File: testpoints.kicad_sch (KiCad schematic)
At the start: 41 parts

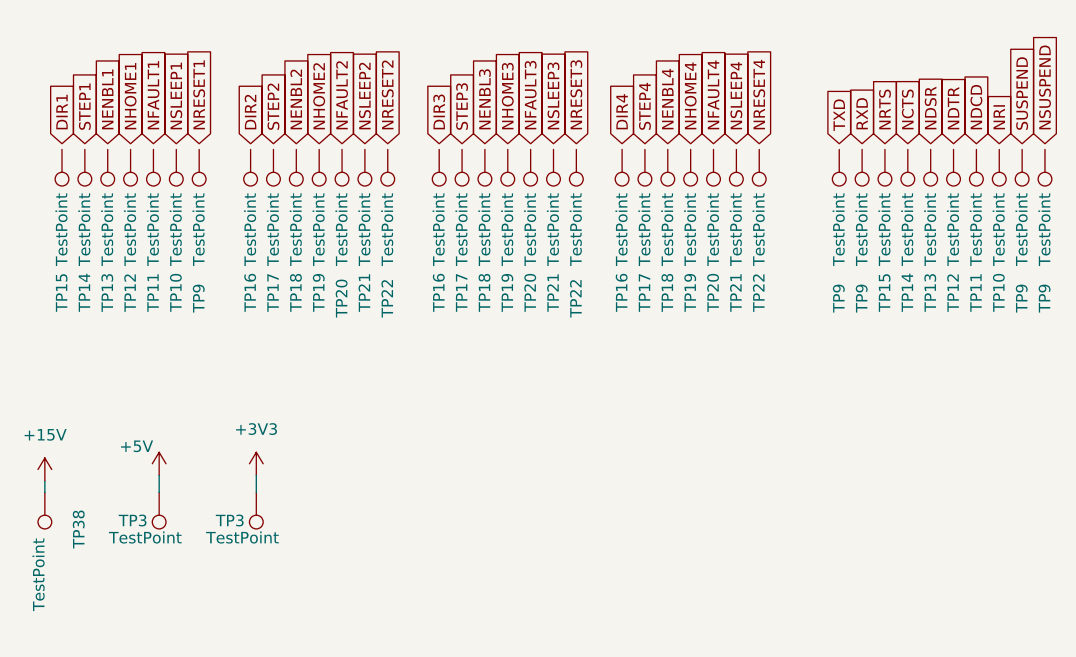
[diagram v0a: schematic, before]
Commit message: routet Motor Driver modules, reattached and placed testpoints
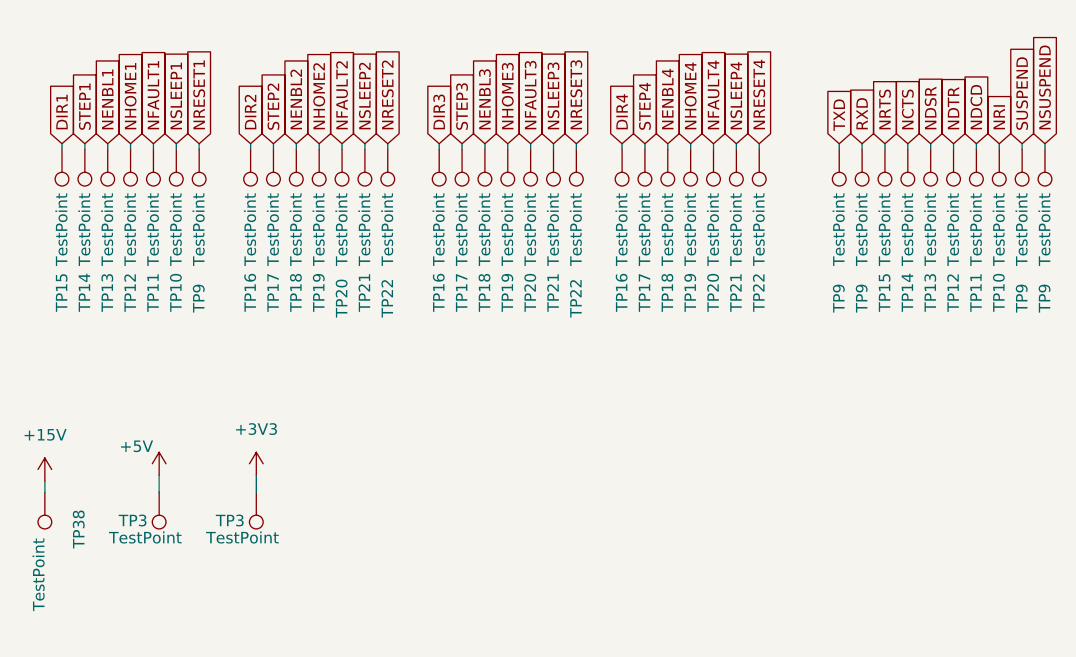
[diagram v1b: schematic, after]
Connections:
- net DIR1: now also TP15.1
- net DIR2: now also TP16.1
- net DIR3: now also TP16.1
- net DIR4: now also TP16.1
- net NCTS: now also TP14.1
- net NDCD: now also TP11.1
- net NDSR: now also TP13.1
- net NDTR: now also TP12.1
- net NENBL1: now also TP13.1
- net NENBL2: now also TP18.1
- net NENBL3: now also TP18.1
- net NENBL4: now also TP18.1
- net NFAULT1: now also TP11.1
- net NFAULT2: now also TP20.1
- net NFAULT3: now also TP20.1
- net NFAULT4: now also TP20.1
- net NHOME1: now also TP12.1
- net NHOME2: now also TP19.1
- net NHOME3: now also TP19.1
- net NHOME4: now also TP19.1
- net NRESET1: now also TP9.1
- net NRESET2: now also TP22.1
- net NRESET3: now also TP22.1
- net NRESET4: now also TP22.1
- net NRI: now also TP10.1
- net NRTS: now also TP15.1
- net NSLEEP1: now also TP10.1
- net NSLEEP2: now also TP21.1
- net NSLEEP3: now also TP21.1
- net NSLEEP4: now also TP21.1
- net NSUSPEND: now also TP9.1
- net RXD: now also TP9.1
- net STEP1: now also TP14.1
- net STEP2: now also TP17.1
- net STEP3: now also TP17.1
- net STEP4: now also TP17.1
- net SUSPEND: now also TP9.1
- net TXD: now also TP9.1
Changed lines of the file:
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@@
 (kicad_sch (version 20230121) (generator eeschema)
   (paper "A4")
+  (wire (pts (xy 53.34 92.71) (xy 53.34 93.345))
+    (stroke (width 0) (type default))
+  )
+  (wire (pts (xy 85.09 92.71) (xy 85.09 93.345))
+    (stroke (width 0) (type default))
+  )
+  (wire (pts (xy 142.24 92.71) (xy 142.24 93.345))
+    (stroke (width 0) (type default))
+  )
+  (wire (pts (xy 64.135 92.71) (xy 64.135 93.345))
+    (stroke (width 0) (type default))
+  )
+  (wire (pts (xy 71.755 92.71) (xy 71.755 93.345))
+    (stroke (width 0) (type default))
+  )
+  (wire (pts (xy 152.4 92.71) (xy 152.4 93.345))
+    (stroke (width 0) (type default))
+  )
+  (wire (pts (xy 55.88 92.71) (xy 55.88 93.345))
+    (stroke (width 0) (type default))
+  )
+  (wire (pts (xy 76.835 92.71) (xy 76.835 93.345))
+    (stroke (width 0) (type default))
+  )
+  (wire (pts (xy 107.95 92.71) (xy 107.95 93.345))
+    (stroke (width 0) (type default))
+  )
+  (wire (pts (xy 50.8 92.71) (xy 50.8 93.345))
+    (stroke (width 0) (type default))
+  )
+  (wire (pts (xy 134.62 92.71) (xy 134.62 93.345))
+    (stroke (width 0) (type default))
+  )
   (wire (pts (xy 53.975 131.445) (xy 53.975 129.54))
+    (stroke (width 0) (type default))
+  )
+  (wire (pts (xy 95.25 92.71) (xy 95.25 93.345))
+    (stroke (width 0) (type default))
+  )
+  (wire (pts (xy 97.79 92.71) (xy 97.79 93.345))
+    (stroke (width 0) (type default))
+  )
+  (wire (pts (xy 100.33 92.71) (xy 100.33 93.345))
+    (stroke (width 0) (type default))
+  )
+  (wire (pts (xy 79.375 92.71) (xy 79.375 93.345))
     (stroke (width 0) (type default))
   )
@@
     (stroke (width 0) (type default))
   )
+  (wire (pts (xy 129.54 92.71) (xy 129.54 93.345))
+    (stroke (width 0) (type default))
+  )
+  (wire (pts (xy 74.295 92.71) (xy 74.295 93.345))
+    (stroke (width 0) (type default))
+  )
+  (wire (pts (xy 147.32 92.71) (xy 147.32 93.345))
+    (stroke (width 0) (type default))
+  )
+  (wire (pts (xy 43.18 92.71) (xy 43.18 93.345))
+    (stroke (width 0) (type default))
+  )
+  (wire (pts (xy 69.215 92.71) (xy 69.215 93.345))
+    (stroke (width 0) (type default))
+  )
+  (wire (pts (xy 45.72 92.71) (xy 45.72 93.345))
+    (stroke (width 0) (type default))
+  )
+  (wire (pts (xy 118.11 92.71) (xy 118.11 93.345))
+    (stroke (width 0) (type default))
+  )
+  (wire (pts (xy 105.41 92.71) (xy 105.41 93.345))
+    (stroke (width 0) (type default))
+  )
+  (wire (pts (xy 113.03 92.71) (xy 113.03 93.345))
+    (stroke (width 0) (type default))
+  )
+  (wire (pts (xy 110.49 92.71) (xy 110.49 93.345))
+    (stroke (width 0) (type default))
+  )
+  (wire (pts (xy 137.16 92.71) (xy 137.16 93.345))
+    (stroke (width 0) (type default))
+  )
+  (wire (pts (xy 66.675 92.71) (xy 66.675 93.345))
+    (stroke (width 0) (type default))
+  )
+  (wire (pts (xy 58.42 92.71) (xy 58.42 93.345))
+    (stroke (width 0) (type default))
+  )
   (wire (pts (xy 64.77 131.445) (xy 64.77 129.54))
     (stroke (width 0) (type default))
   )
+  (wire (pts (xy 120.65 92.71) (xy 120.65 93.345))
+    (stroke (width 0) (type default))
+  )
+  (wire (pts (xy 115.57 92.71) (xy 115.57 93.345))
+    (stroke (width 0) (type default))
+  )
+  (wire (pts (xy 48.26 92.71) (xy 48.26 93.345))
+    (stroke (width 0) (type default))
+  )
+  (wire (pts (xy 149.86 92.71) (xy 149.86 93.345))
+    (stroke (width 0) (type default))
+  )
+  (wire (pts (xy 139.7 92.71) (xy 139.7 93.345))
+    (stroke (width 0) (type default))
+  )
+  (wire (pts (xy 132.08 92.71) (xy 132.08 93.345))
+    (stroke (width 0) (type default))
+  )
+  (wire (pts (xy 92.71 92.71) (xy 92.71 93.345))
+    (stroke (width 0) (type default))
+  )
+  (wire (pts (xy 87.63 92.71) (xy 87.63 93.345))
+    (stroke (width 0) (type default))
+  )
+  (wire (pts (xy 144.78 92.71) (xy 144.78 93.345))
+    (stroke (width 0) (type default))
+  )
+  (wire (pts (xy 90.17 92.71) (xy 90.17 93.345))
+    (stroke (width 0) (type default))
+  )

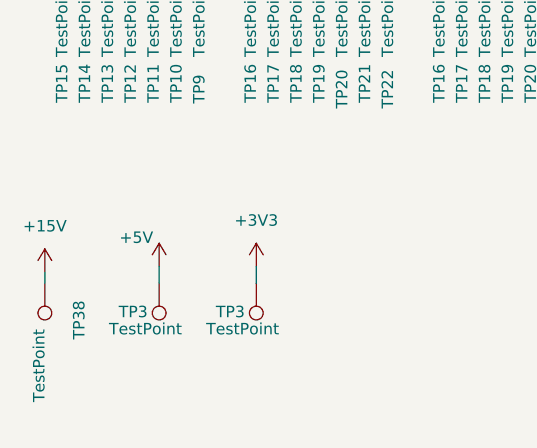
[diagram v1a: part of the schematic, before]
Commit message: finished PCB. DRC 0 errors
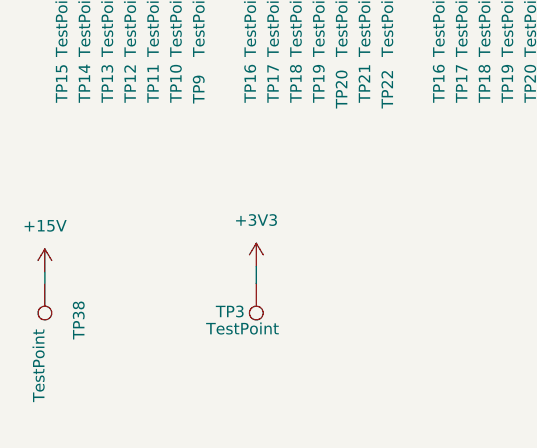
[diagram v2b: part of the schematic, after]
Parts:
- removed TP3: TestPoint, TestPoint:TestPoint_Pad_D2.5mm, symbol Connector:TestPoint
- TP10, TP11, TP12, TP13, TP14, TP15, TP16, TP17, TP18, TP19, TP20, TP21, TP22, TP3, TP38, TP9: footprint TestPoint:TestPoint_Pad_D2.5mm -> TestPoint:TestPoint_Pad_D1.5mm

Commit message: completly reroutet EVERYTHING
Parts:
- removed TP10 (x2), TP11 (x2), TP12 (x2), TP13 (x2), TP14 (x2), TP15 (x2), TP16 (x3), TP17 (x3), TP18 (x3), TP19 (x3), TP20 (x3), TP21 (x3), TP22 (x3), TP3, TP38, TP9 (x5): TestPoint, TestPoint:TestPoint_Pad_D1.5mm, symbol Connector:TestPoint

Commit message: moved every third party content to lib, added 3d models and also just finished rerouting EVERYTHING. also added pcb addon for st-link so i dont accidentally verole anymore
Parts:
- added J4: PINHD_1x4_Male, Connector_PinHeader_2.54mm:PinHeader_1x04_P2.54mm_Vertical, symbol PCM_SL_Pin_Headers:PINHD_1x4_Male
- added J5: USB_A, Connector_USB:USB_A_Stewart_SS-52100-001_Horizontal, symbol Connector:USB_A
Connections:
- new net: J4.1, J5.3 (D+)
- new net: J4.2, J5.4 (GND), J5.5 (Shield)
- new net: J4.3, J5.2 (D-)
- new net: J4.4, J5.1 (VBUS)
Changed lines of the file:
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@@
 (kicad_sch (version 20230121) (generator eeschema)
   (paper "A4")
+  (junction (at 101.6 118.11) (diameter 0) (color 0 0 0 0)
+  )
+  (wire (pts (xy 89.535 111.76) (xy 89.535 101.6))
+    (stroke (width 0) (type default))
+  )
+  (wire (pts (xy 102.87 116.84) (xy 102.87 118.11))
+    (stroke (width 0) (type default))
+  )
+  (wire (pts (xy 101.6 118.11) (xy 100.33 118.11))
+    (stroke (width 0) (type default))
+  )
+  (wire (pts (xy 88.265 104.14) (xy 92.71 104.14))
+    (stroke (width 0) (type default))
+  )
+  (wire (pts (xy 89.535 101.6) (xy 92.71 101.6))
+    (stroke (width 0) (type default))
+  )
+  (wire (pts (xy 88.265 109.22) (xy 92.71 109.22))
+    (stroke (width 0) (type default))
+  )
+  (wire (pts (xy 100.33 118.11) (xy 100.33 116.84))
+    (stroke (width 0) (type default))
+  )
+  (wire (pts (xy 88.265 106.68) (xy 90.805 106.68))
+    (stroke (width 0) (type default))
+  )
+  (wire (pts (xy 92.71 104.14) (xy 92.71 106.68))
+    (stroke (width 0) (type default))
+  )
+  (wire (pts (xy 90.805 106.68) (xy 90.805 120.015))
+    (stroke (width 0) (type default))
+  )
+  (wire (pts (xy 90.805 120.015) (xy 101.6 120.015))
+    (stroke (width 0) (type default))
+  )
+  (wire (pts (xy 101.6 120.015) (xy 101.6 118.11))
+    (stroke (width 0) (type default))
+  )
+  (wire (pts (xy 101.6 118.11) (xy 102.87 118.11))
+    (stroke (width 0) (type default))
+  )
+  (wire (pts (xy 88.265 111.76) (xy 89.535 111.76))
+    (stroke (width 0) (type default))
+  )
+  (symbol (lib_id "PCM_SL_Pin_Headers:PINHD_1x4_Male") (at 84.455 107.95 0) (mirror y) (unit 1)
+    (in_bom yes) (on_board yes) (dnp no) (fields_autoplaced)
+    (property "Reference" "J4" (at 81.915 106.68 0)
+      (effects (font (size 1.27 1.27)) (justify left))
+    )
+    (property "Value" "PINHD_1x4_Male" (at 81.915 109.22 0)
+      (effects (font (size 1.27 1.27)) (justify left))
+    )
+    (property "Footprint" "Connector_PinHeader_2.54mm:PinHeader_1x04_P2.54mm_Vertical" (at 85.725 96.52 0)
+      (effects (font (size 1.27 1.27)) hide)
+    )
+    (property "Datasheet" "" (at 84.455 97.79 0)
+      (effects (font (size 1.27 1.27)) hide)
+    )
+    (pin "3")
+    (pin "4")
+    (pin "2")
+    (pin "1")
+    (instances
+      (project "Doodle Drive"
+        (path "/3ec634aa-8c09-482d-9325-2288a4dbd68b/bef0954e-6024-4756-b9a6-5ea2a0825f13"
+          (reference "J4") (unit 1)
+        )
+      )
+    )
+  )
+  (symbol (lib_id "Connector:USB_A") (at 100.33 106.68 0) (mirror y) (unit 1)
+    (in_bom yes) (on_board yes) (dnp no) (fields_autoplaced)
+    (property "Reference" "J5" (at 100.33 94.615 0)
+      (effects (font (size 1.27 1.27)))
+    )
+    (property "Value" "USB_A" (at 100.33 97.155 0)
+      (effects (font (size 1.27 1.27)))
+    )
+    (property "Footprint" "Connector_USB:USB_A_Stewart_SS-52100-001_Horizontal" (at 96.52 107.95 0)
+      (effects (font (size 1.27 1.27)) hide)
+    )
+    (property "Datasheet" " ~" (at 96.52 107.95 0)
+      (effects (font (size 1.27 1.27)) hide)
+    )
+    (pin "5")
+    (pin "1")
+    (pin "2")
+    (pin "3")
+    (pin "4")
+    (instances
+      (project "Doodle Drive"
+        (path "/3ec634aa-8c09-482d-9325-2288a4dbd68b/bef0954e-6024-4756-b9a6-5ea2a0825f13"
+          (reference "J5") (unit 1)
+        )
+      )
+    )
+  )
 )

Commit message: fixed variuopus stuff, this is probaly the bestellte version
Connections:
- net at J4.1: now also J5.1 (VBUS); no longer J5.3 (D+)
- net at J5.4 (GND), J5.5 (Shield): now also J4.3; no longer J4.2
- net at J5.2 (D-): now also J4.2; no longer J4.3
- net at J4.4: now also J5.3 (D+); no longer J5.1 (VBUS)
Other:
- moved on the sheet: J4
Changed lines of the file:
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@@
     (stroke (width 0) (type default))
   )
-  (wire (pts (xy 88.265 104.14) (xy 92.71 104.14))
+  (wire (pts (xy 88.265 104.14) (xy 92.075 104.14))
     (stroke (width 0) (type default))
   )
@@
     (stroke (width 0) (type default))
   )
-  (wire (pts (xy 92.71 104.14) (xy 92.71 106.68))
+  (wire (pts (xy 92.075 104.14) (xy 92.075 106.68))
     (stroke (width 0) (type default))
   )
@@
     (stroke (width 0) (type default))
   )
+  (wire (pts (xy 92.075 106.68) (xy 92.71 106.68))
+    (stroke (width 0) (type default))
+  )
   (wire (pts (xy 88.265 111.76) (xy 89.535 111.76))
     (stroke (width 0) (type default))
   )
-  (symbol (lib_id "PCM_SL_Pin_Headers:PINHD_1x4_Male") (at 84.455 107.95 0) (mirror y) (unit 1)
-    (in_bom yes) (on_board yes) (dnp no) (fields_autoplaced)
-    (property "Reference" "J4" (at 81.915 106.68 0)
+  (symbol (lib_id "PCM_SL_Pin_Headers:PINHD_1x4_Male") (at 84.455 107.95 180) (unit 1)
+    (in_bom yes) (on_board yes) (dnp no)
+    (property "Reference" "J4" (at 81.915 109.22 0)
       (effects (font (size 1.27 1.27)) (justify left))
     )
-    (property "Value" "PINHD_1x4_Male" (at 81.915 109.22 0)
+    (property "Value" "PINHD_1x4_Male" (at 81.915 106.68 0)
       (effects (font (size 1.27 1.27)) (justify left))
     )
-    (property "Footprint" "Connector_PinHeader_2.54mm:PinHeader_1x04_P2.54mm_Vertical" (at 85.725 96.52 0)
+    (property "Footprint" "Connector_PinHeader_2.54mm:PinHeader_1x04_P2.54mm_Vertical" (at 85.725 119.38 0)
       (effects (font (size 1.27 1.27)) hide)
     )
-    (property "Datasheet" "" (at 84.455 97.79 0)
+    (property "Datasheet" "" (at 84.455 118.11 0)
       (effects (font (size 1.27 1.27)) hide)
     )

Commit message: added pins for motor edge sensors, reroutet driver modules, removed module potentiometer, made everything more compact, fixed labels
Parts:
- removed J4: PINHD_1x4_Male, Connector_PinHeader_2.54mm:PinHeader_1x04_P2.54mm_Vertical, symbol PCM_SL_Pin_Headers:PINHD_1x4_Male
- removed J5: USB_A, Connector_USB:USB_A_Stewart_SS-52100-001_Horizontal, symbol Connector:USB_A
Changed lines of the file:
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@@
 (kicad_sch (version 20230121) (generator eeschema)
   (paper "A4")
-  (junction (at 101.6 118.11) (diameter 0) (color 0 0 0 0)
-  )
-  (wire (pts (xy 89.535 111.76) (xy 89.535 101.6))
-    (stroke (width 0) (type default))
-  )
-  (wire (pts (xy 102.87 116.84) (xy 102.87 118.11))
-    (stroke (width 0) (type default))
-  )
-  (wire (pts (xy 101.6 118.11) (xy 100.33 118.11))
-    (stroke (width 0) (type default))
-  )
-  (wire (pts (xy 88.265 104.14) (xy 92.075 104.14))
-    (stroke (width 0) (type default))
-  )
-  (wire (pts (xy 89.535 101.6) (xy 92.71 101.6))
-    (stroke (width 0) (type default))
-  )
-  (wire (pts (xy 88.265 109.22) (xy 92.71 109.22))
-    (stroke (width 0) (type default))
-  )
-  (wire (pts (xy 100.33 118.11) (xy 100.33 116.84))
-    (stroke (width 0) (type default))
-  )
-  (wire (pts (xy 88.265 106.68) (xy 90.805 106.68))
-    (stroke (width 0) (type default))
-  )
-  (wire (pts (xy 92.075 104.14) (xy 92.075 106.68))
-    (stroke (width 0) (type default))
-  )
-  (wire (pts (xy 90.805 106.68) (xy 90.805 120.015))
-    (stroke (width 0) (type default))
-  )
-  (wire (pts (xy 90.805 120.015) (xy 101.6 120.015))
-    (stroke (width 0) (type default))
-  )
-  (wire (pts (xy 101.6 120.015) (xy 101.6 118.11))
-    (stroke (width 0) (type default))
-  )
-  (wire (pts (xy 101.6 118.11) (xy 102.87 118.11))
-    (stroke (width 0) (type default))
-  )
-  (wire (pts (xy 92.075 106.68) (xy 92.71 106.68))
-    (stroke (width 0) (type default))
-  )
-  (wire (pts (xy 88.265 111.76) (xy 89.535 111.76))
-    (stroke (width 0) (type default))
-  )
-  (symbol (lib_id "PCM_SL_Pin_Headers:PINHD_1x4_Male") (at 84.455 107.95 180) (unit 1)
-    (in_bom yes) (on_board yes) (dnp no)
-    (property "Reference" "J4" (at 81.915 109.22 0)
-      (effects (font (size 1.27 1.27)) (justify left))
-    )
-    (property "Value" "PINHD_1x4_Male" (at 81.915 106.68 0)
-      (effects (font (size 1.27 1.27)) (justify left))
-    )
-    (property "Footprint" "Connector_PinHeader_2.54mm:PinHeader_1x04_P2.54mm_Vertical" (at 85.725 119.38 0)
-      (effects (font (size 1.27 1.27)) hide)
-    )
-    (property "Datasheet" "" (at 84.455 118.11 0)
-      (effects (font (size 1.27 1.27)) hide)
-    )
-    (pin "3")
-    (pin "4")
-    (pin "2")
-    (pin "1")
-    (instances
-      (project "Doodle Drive"
-        (path "/3ec634aa-8c09-482d-9325-2288a4dbd68b/bef0954e-6024-4756-b9a6-5ea2a0825f13"
-          (reference "J4") (unit 1)
-        )
-      )
-    )
-  )
-  (symbol (lib_id "Connector:USB_A") (at 100.33 106.68 0) (mirror y) (unit 1)
-    (in_bom yes) (on_board yes) (dnp no) (fields_autoplaced)
-    (property "Reference" "J5" (at 100.33 94.615 0)
-      (effects (font (size 1.27 1.27)))
-    )
-    (property "Value" "USB_A" (at 100.33 97.155 0)
-      (effects (font (size 1.27 1.27)))
-    )
-    (property "Footprint" "Connector_USB:USB_A_Stewart_SS-52100-001_Horizontal" (at 96.52 107.95 0)
-      (effects (font (size 1.27 1.27)) hide)
-    )
-    (property "Datasheet" " ~" (at 96.52 107.95 0)
-      (effects (font (size 1.27 1.27)) hide)
-    )
-    (pin "5")
-    (pin "1")
-    (pin "2")
-    (pin "3")
-    (pin "4")
-    (instances
-      (project "Doodle Drive"
-        (path "/3ec634aa-8c09-482d-9325-2288a4dbd68b/bef0954e-6024-4756-b9a6-5ea2a0825f13"
-          (reference "J5") (unit 1)
-        )
-      )
-    )
-  )
 )
